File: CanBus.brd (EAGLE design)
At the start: 80 x 100 mm, 59 parts, among them IC1 MCP2515-I/SO, IC2 MEGA8-AI, IC3 MCP2515-I/SO, Q1 16MHz, Q2 16MHz, Q3 16MHz, U1 MCP2562-E/SN, U2 MCP2562-E/SN, X1 MAC64L

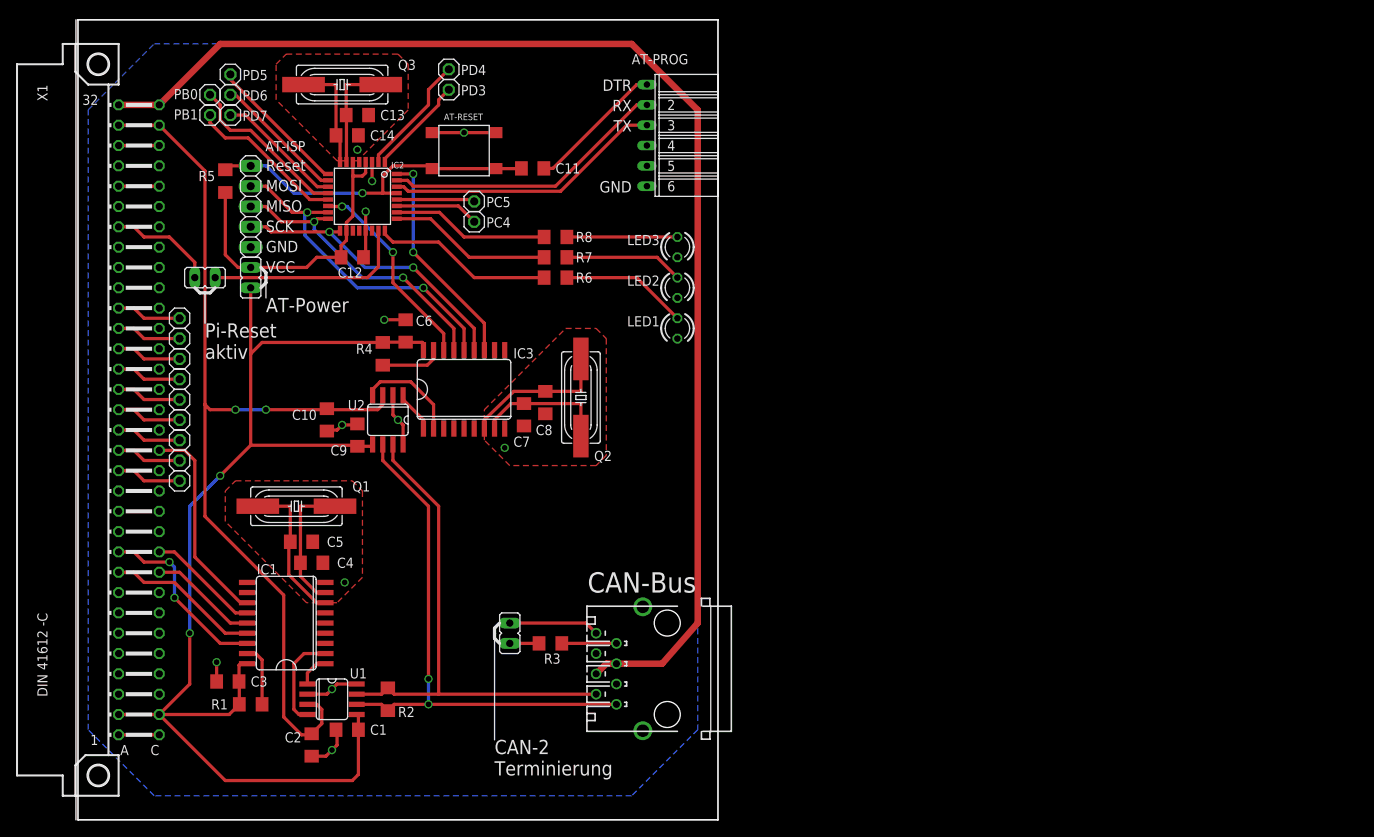
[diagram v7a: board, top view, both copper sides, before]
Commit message: CAN-Bus Beadboard-Adapter, Layouts angepasst
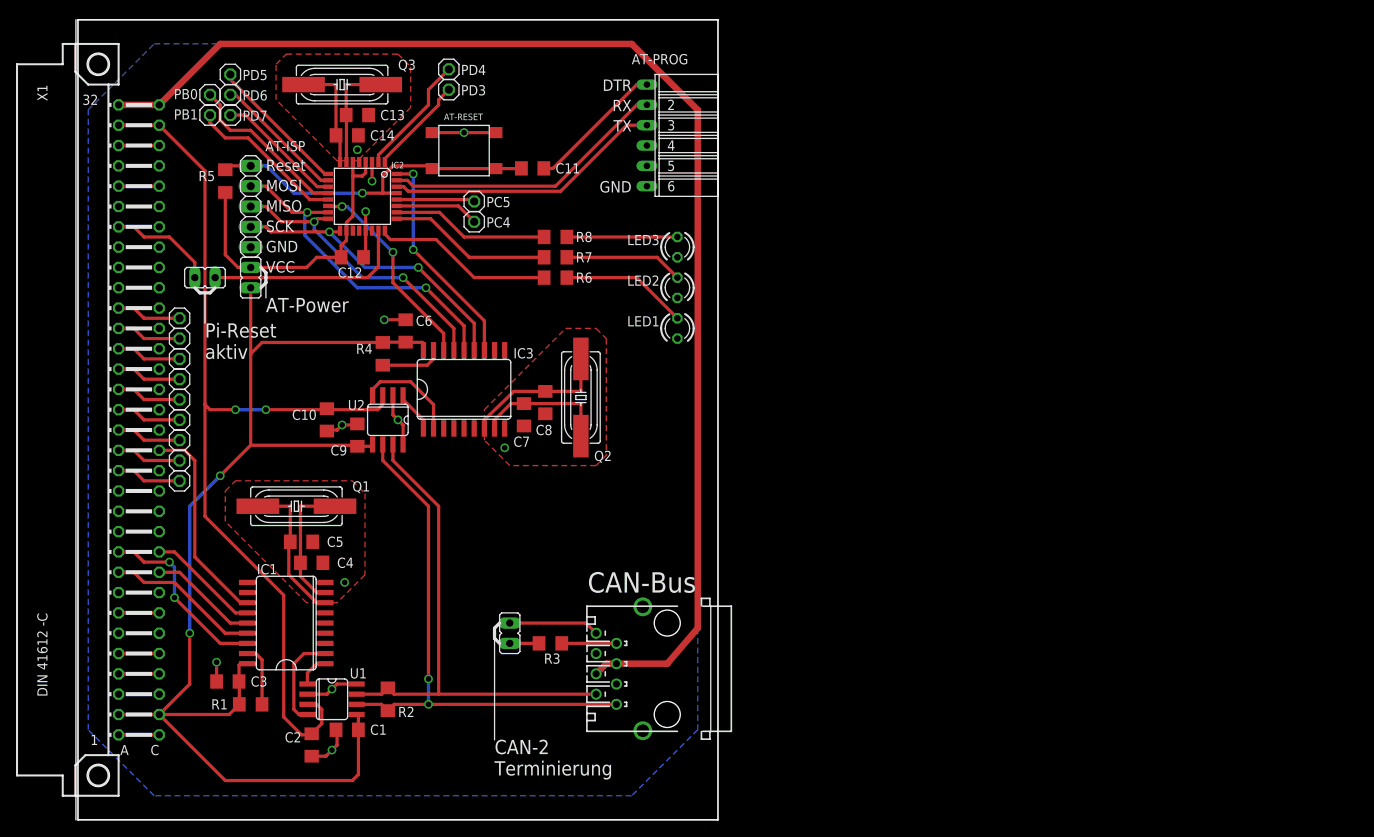
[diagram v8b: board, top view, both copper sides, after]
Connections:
- removed net N$12: X1.A4
- removed net N$16: X1.A7
- removed net N$8: X1.A5
- net 1WIRE: now also X1.A7
- net I2C_SCL: now also X1.A5
- net I2C_SDA: now also X1.A4
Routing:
- net I2C_SDA: track 0.00 -> 5.08 mm
- net I2C_SCL: track 0.00 -> 5.08 mm
- net 1WIRE: track 0.00 -> 5.08 mm
